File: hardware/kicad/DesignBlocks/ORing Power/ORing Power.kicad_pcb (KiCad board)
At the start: 2 copper layers, 39 x 15 mm, 13 parts, among them J1 Conn_01x02_Pin, J3 USB_C_Receptacle_PowerOnly_6P, U1 LM3940IMP-3.3/NOPB, U2 ORingPower_Module

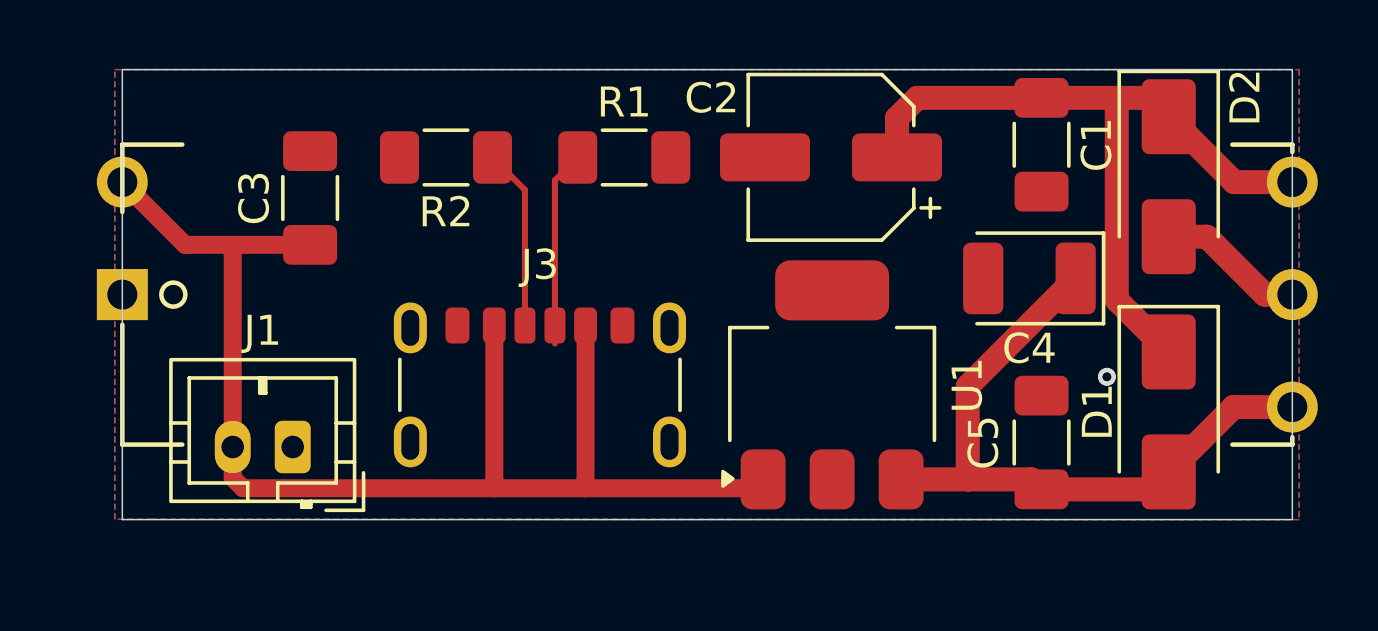
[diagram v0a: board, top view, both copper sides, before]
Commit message: fix(hardware): use SMD JST-PH on ORing power module
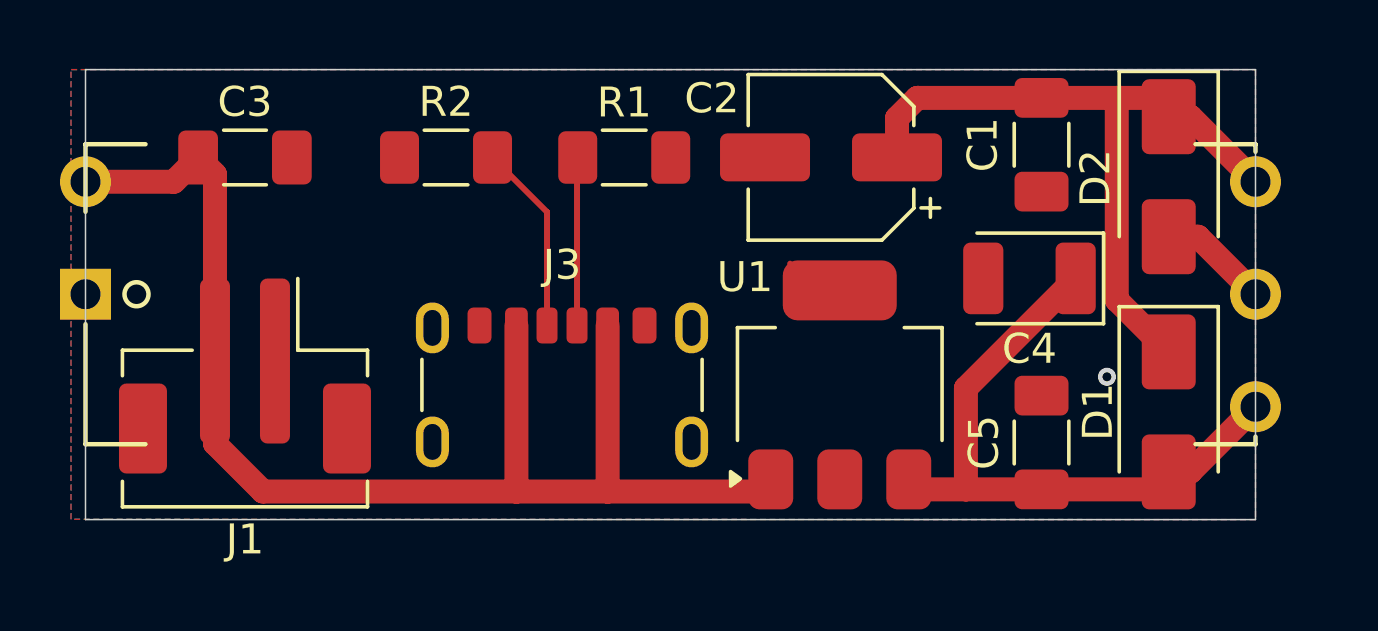
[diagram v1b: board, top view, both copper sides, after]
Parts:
- J1: footprint Connector_JST:JST_PH_B2B-PH-K_1x02_P2.00mm_Vertical -> Connector_JST:JST_PH_B2B-PH-SM4-TB_1x02-1MP_P2.00mm_Vertical
- moved J1 2.85 mm to (114.4, 103.6)
- moved C3 2.56 mm to (114.4, 96.3), turned to 0 degrees
- moved U2 1.23 mm to (128.6, 100.9)
- moved J3 0.74 mm to (125.0, 105.0)
- moved U1 0.25 mm to (134.2, 103.9)
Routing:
- net +3V3_DEVKIT: track 4.93 -> 3.69 mm
- net +3V3_SYS: track 25.1 -> 23.9 mm
- net +3V3_EXT: track 22.5 -> 21.4 mm
- net +5V: track 43.7 -> 44.7 mm
- net Net-(J3-CC2): track 7.12 -> 6.22 mm
